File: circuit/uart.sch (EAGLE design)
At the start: 2 parts

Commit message: New circuit
Hopefully the final
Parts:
- added R3, R4: 1K, resistor:R-US_0204/5
- R1: value 4K7 -> 1K; device resistor:R-US_0204/7 -> resistor:R-US_0204/5
- R2: value 10K -> 1K; device resistor:R-US_0204/7 -> resistor:R-US_0204/5
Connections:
- removed net 0V: R1.1, R2.1
- new net GND: R2.1, R4.1
- new net N$2: R1.1, R2.2
- new net N$3: R3.2
- new net N$4: R3.1, R4.2
- net N$1: no longer R2.2
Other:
- note added: "AVR RX"
- note added: "AVR TX"
- note added: "RaspberryPi RX"
- note added: "RaspberryPi TX"
- note removed: "Metal contacts"
- note removed: "ONEWIRE_P"
- note removed: "onewire_pins[]"
- note removed: "station"
- note removed: "train"
- moved on the sheet: R1, R2
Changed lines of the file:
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@@
 </classes>
 <parts>
-<part name="R1" library="resistor" deviceset="R-US_" device="0204/7" value="4K7"/>
-<part name="R2" library="resistor" deviceset="R-US_" device="0204/7" value="10K"/>
-<part name="GND1" library="supply1" deviceset="0V" device=""/>
-<part name="GND2" library="supply1" deviceset="0V" device=""/>
+<part name="R1" library="resistor" deviceset="R-US_" device="0204/5" value="1K"/>
+<part name="R2" library="resistor" deviceset="R-US_" device="0204/5" value="1K"/>
+<part name="R3" library="resistor" deviceset="R-US_" device="0204/5" value="1K"/>
+<part name="R4" library="resistor" deviceset="R-US_" device="0204/5" value="1K"/>
+<part name="GND1" library="supply1" deviceset="GND" device=""/>
+<part name="GND2" library="supply1" deviceset="GND" device=""/>
 <part name="SUPPLY1" library="supply2" deviceset="V--&gt;" device=""/>
-<part name="SUPPLY2" library="supply2" deviceset="V&lt;--" device=""/>
+<part name="SUPPLY2" library="supply2" deviceset="V--&gt;" device=""/>
+<part name="SUPPLY3" library="supply2" deviceset="V&lt;--" device=""/>
+<part name="SUPPLY4" library="supply2" deviceset="V&lt;--" device=""/>
 </parts>
 <sheets>
 <sheet>
 <plain>
-<text x="33.02" y="68.58" size="1.778" layer="97">ONEWIRE_P</text>
-<text x="-30.48" y="68.58" size="1.778" layer="97">onewire_pins[]</text>
-<text x="0" y="66.04" size="1.778" layer="97">Metal contacts</text>
-<text x="-27.94" y="60.96" size="1.778" layer="97">station</text>
-<text x="38.1" y="60.96" size="1.778" layer="97">train</text>
+<text x="22.86" y="76.2" size="1.778" layer="97">AVR TX</text>
+<text x="22.86" y="33.02" size="1.778" layer="97">AVR RX</text>
+<text x="63.5" y="15.24" size="1.778" layer="97">RaspberryPi TX</text>
+<text x="60.96" y="58.42" size="1.778" layer="97">RaspberryPi RX</text>
 </plain>
 <instances>
-<instance part="R1" gate="G$1" x="-7.62" y="58.42" rot="R90"/>
-<instance part="R2" gate="G$1" x="22.86" y="58.42" rot="R90"/>
-<instance part="GND1" gate="1" x="-7.62" y="45.72"/>
-<instance part="GND2" gate="1" x="22.86" y="45.72"/>
-<instance part="SUPPLY1" gate="G$1" x="-30.48" y="66.04"/>
-<instance part="SUPPLY2" gate="G$1" x="48.26" y="66.04"/>
+<instance part="R1" gate="G$1" x="50.8" y="63.5" rot="R90"/>
+<instance part="R2" gate="G$1" x="50.8" y="48.26" rot="R90"/>
+<instance part="R3" gate="G$1" x="50.8" y="20.32" rot="R90"/>
+<instance part="R4" gate="G$1" x="50.8" y="5.08" rot="R90"/>
+<instance part="GND1" gate="1" x="50.8" y="35.56"/>
+<instance part="GND2" gate="1" x="50.8" y="-7.62"/>
+<instance part="SUPPLY1" gate="G$1" x="20.32" y="73.66"/>
+<instance part="SUPPLY2" gate="G$1" x="20.32" y="30.48"/>
+<instance part="SUPPLY3" gate="G$1" x="78.74" y="12.7"/>
+<instance part="SUPPLY4" gate="G$1" x="76.2" y="55.88"/>
 </instances>
 <busses>
@@
 <net name="N$1" class="0">
 <segment>
-<wire x1="-15.24" y1="66.04" x2="-7.62" y2="66.04" width="0.1524" layer="91"/>
 <pinref part="R1" gate="G$1" pin="2"/>
-<wire x1="33.02" y1="66.04" x2="22.86" y2="66.04" width="0.1524" layer="91"/>
-<wire x1="22.86" y1="66.04" x2="-7.62" y2="66.04" width="0.1524" layer="91"/>
-<wire x1="-7.62" y1="66.04" x2="-7.62" y2="63.5" width="0.1524" layer="91"/>
-<pinref part="R2" gate="G$1" pin="2"/>
-<wire x1="22.86" y1="66.04" x2="22.86" y2="63.5" width="0.1524" layer="91"/>
-<junction x="22.86" y="66.04"/>
-<junction x="-7.62" y="66.04"/>
+<wire x1="35.56" y1="73.66" x2="50.8" y2="73.66" width="0.1524" layer="91"/>
+<wire x1="50.8" y1="73.66" x2="50.8" y2="68.58" width="0.1524" layer="91"/>
 </segment>
 </net>
-<net name="0V" class="0">
+<net name="N$2" class="0">
 <segment>
 <pinref part="R1" gate="G$1" pin="1"/>
-<pinref part="GND1" gate="1" pin="0V"/>
-<wire x1="-7.62" y1="53.34" x2="-7.62" y2="48.26" width="0.1524" layer="91"/>
+<pinref part="R2" gate="G$1" pin="2"/>
+<wire x1="50.8" y1="58.42" x2="50.8" y2="55.88" width="0.1524" layer="91"/>
+<wire x1="50.8" y1="55.88" x2="50.8" y2="53.34" width="0.1524" layer="91"/>
+<wire x1="60.96" y1="55.88" x2="50.8" y2="55.88" width="0.1524" layer="91"/>
+<junction x="50.8" y="55.88"/>
+</segment>
+</net>
+<net name="GND" class="0">
+<segment>
+<pinref part="R2" gate="G$1" pin="1"/>
+<pinref part="GND1" gate="1" pin="GND"/>
+<wire x1="50.8" y1="43.18" x2="50.8" y2="38.1" width="0.1524" layer="91"/>
 </segment>
 <segment>
-<pinref part="R2" gate="G$1" pin="1"/>
-<pinref part="GND2" gate="1" pin="0V"/>
-<wire x1="22.86" y1="53.34" x2="22.86" y2="48.26" width="0.1524" layer="91"/>
+<pinref part="R4" gate="G$1" pin="1"/>
+<pinref part="GND2" gate="1" pin="GND"/>
+<wire x1="50.8" y1="0" x2="50.8" y2="-5.08" width="0.1524" layer="91"/>
 </segment>
 </net>
+<net name="N$3" class="0">
+<segment>
+<pinref part="R3" gate="G$1" pin="2"/>
+<wire x1="50.8" y1="25.4" x2="50.8" y2="30.48" width="0.1524" layer="91"/>
+<wire x1="50.8" y1="30.48" x2="35.56" y2="30.48" width="0.1524" layer="91"/>
+</segment>
+</net>
+<net name="N$4" class="0">
+<segment>
+<pinref part="R3" gate="G$1" pin="1"/>
+<pinref part="R4" gate="G$1" pin="2"/>
+<wire x1="50.8" y1="15.24" x2="50.8" y2="12.7" width="0.1524" layer="91"/>
+<wire x1="50.8" y1="12.7" x2="50.8" y2="10.16" width="0.1524" layer="91"/>
+<wire x1="63.5" y1="12.7" x2="50.8" y2="12.7" width="0.1524" layer="91"/>
+<junction x="50.8" y="12.7"/>
+</segment>
+</net>

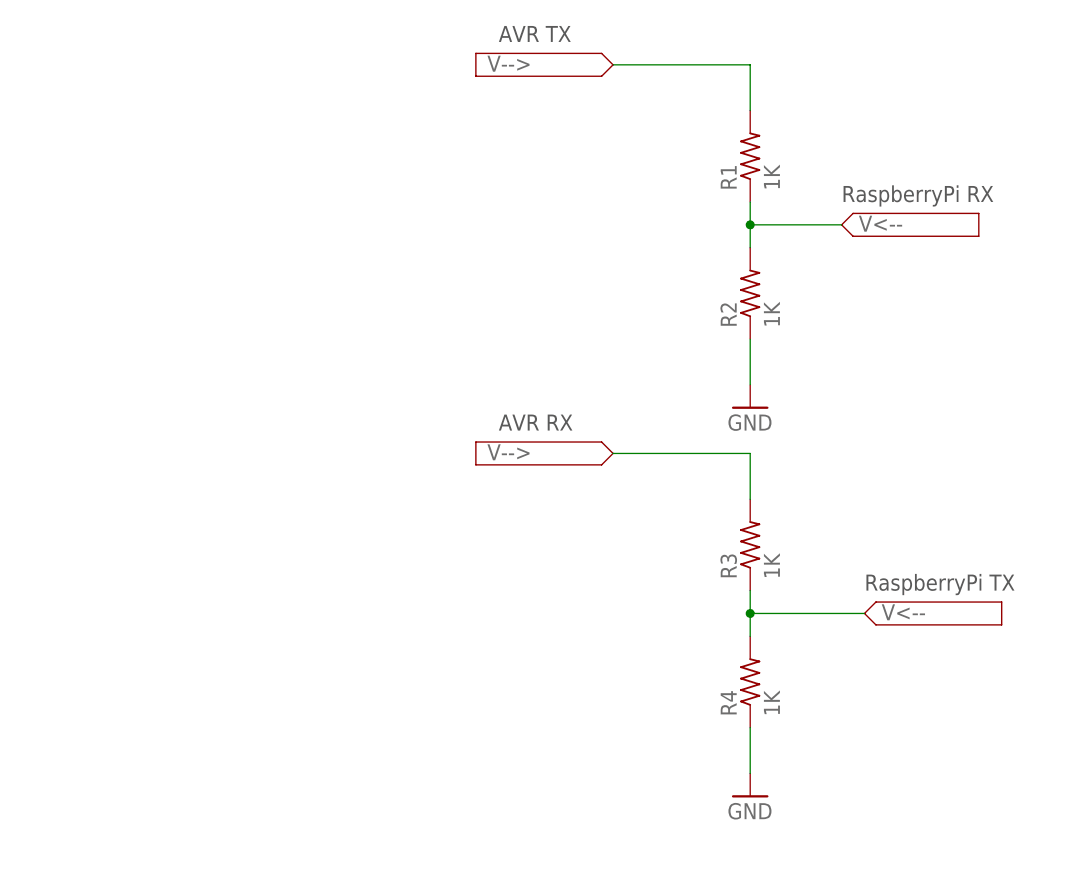
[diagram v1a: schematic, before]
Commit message: New UART circuit
Using CD4050 IC
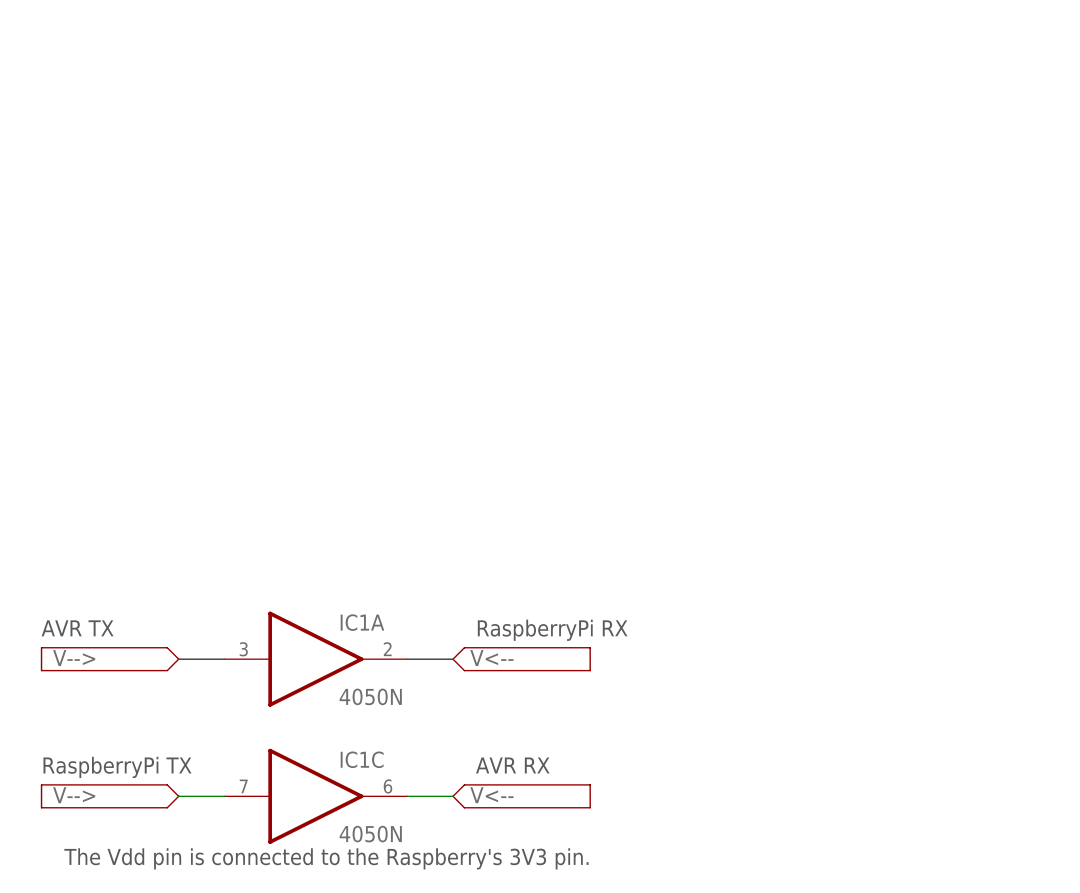
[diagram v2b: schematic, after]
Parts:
- removed R1, R2, R3, R4: 1K, resistor:R-US_0204/5
- added IC1: 4050N, 40xx:4050N
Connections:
- removed net GND: R2.1, R4.1
- net N$1: now also IC1A.I; no longer R1.2
- net N$2: now also IC1C.I; no longer R1.1, R2.2
- net N$3: now also IC1A.O; no longer R3.2
- net N$4: now also IC1C.O; no longer R3.1, R4.2
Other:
- note added: "The Vdd pin is connected to the Raspberry's 3V3 pin."
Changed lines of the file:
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@@
 <setting verticaltext="up"/>
 </settings>
-<grid distance="0.1" unitdist="inch" unit="inch" style="lines" multiple="1" display="no" altdistance="0.01" altunitdist="inch" altunit="inch"/>
+<grid distance="0.1" unitdist="inch" unit="inch" style="lines" multiple="1" display="yes" altdistance="0.01" altunitdist="inch" altunit="inch"/>
 <layers>
 <layer number="1" name="Top" color="4" fill="1" visible="no" active="no"/>
@@
 </classes>
 <parts>
-<part name="R1" library="resistor" deviceset="R-US_" device="0204/5" value="1K"/>
-<part name="R2" library="resistor" deviceset="R-US_" device="0204/5" value="1K"/>
-<part name="R3" library="resistor" deviceset="R-US_" device="0204/5" value="1K"/>
-<part name="R4" library="resistor" deviceset="R-US_" device="0204/5" value="1K"/>
-<part name="GND1" library="supply1" deviceset="GND" device=""/>
-<part name="GND2" library="supply1" deviceset="GND" device=""/>
 <part name="SUPPLY1" library="supply2" deviceset="V--&gt;" device=""/>
 <part name="SUPPLY2" library="supply2" deviceset="V--&gt;" device=""/>
 <part name="SUPPLY3" library="supply2" deviceset="V&lt;--" device=""/>
 <part name="SUPPLY4" library="supply2" deviceset="V&lt;--" device=""/>
+<part name="IC1" library="40xx" deviceset="4050" device="N"/>
 </parts>
 <sheets>
 <sheet>
 <plain>
-<text x="22.86" y="76.2" size="1.778" layer="97">AVR TX</text>
-<text x="22.86" y="33.02" size="1.778" layer="97">AVR RX</text>
-<text x="63.5" y="15.24" size="1.778" layer="97">RaspberryPi TX</text>
-<text x="60.96" y="58.42" size="1.778" layer="97">RaspberryPi RX</text>
+<text x="-27.94" y="10.16" size="1.778" layer="97">AVR TX</text>
+<text x="20.32" y="-5.08" size="1.778" layer="97">AVR RX</text>
+<text x="-27.94" y="-5.08" size="1.778" layer="97">RaspberryPi TX</text>
+<text x="20.32" y="10.16" size="1.778" layer="97">RaspberryPi RX</text>
+<text x="-25.4" y="-15.24" size="1.778" layer="97">The Vdd pin is connected to the Raspberry's 3V3 pin.</text>
 </plain>
 <instances>
-<instance part="R1" gate="G$1" x="50.8" y="63.5" rot="R90"/>
-<instance part="R2" gate="G$1" x="50.8" y="48.26" rot="R90"/>
-<instance part="R3" gate="G$1" x="50.8" y="20.32" rot="R90"/>
-<instance part="R4" gate="G$1" x="50.8" y="5.08" rot="R90"/>
-<instance part="GND1" gate="1" x="50.8" y="35.56"/>
-<instance part="GND2" gate="1" x="50.8" y="-7.62"/>
-<instance part="SUPPLY1" gate="G$1" x="20.32" y="73.66"/>
-<instance part="SUPPLY2" gate="G$1" x="20.32" y="30.48"/>
-<instance part="SUPPLY3" gate="G$1" x="78.74" y="12.7"/>
-<instance part="SUPPLY4" gate="G$1" x="76.2" y="55.88"/>
+<instance part="SUPPLY1" gate="G$1" x="-27.94" y="7.62"/>
+<instance part="SUPPLY2" gate="G$1" x="-27.94" y="-7.62"/>
+<instance part="SUPPLY3" gate="G$1" x="33.02" y="-7.62"/>
+<instance part="SUPPLY4" gate="G$1" x="33.02" y="7.62"/>
+<instance part="IC1" gate="A" x="2.54" y="7.62"/>
+<instance part="IC1" gate="C" x="2.54" y="-7.62"/>
 </instances>
 <busses>
@@
 <net name="N$1" class="0">
 <segment>
-<pinref part="R1" gate="G$1" pin="2"/>
-<wire x1="35.56" y1="73.66" x2="50.8" y2="73.66" width="0.1524" layer="91"/>
-<wire x1="50.8" y1="73.66" x2="50.8" y2="68.58" width="0.1524" layer="91"/>
+<pinref part="IC1" gate="A" pin="I"/>
+<wire x1="-12.7" y1="7.62" x2="-7.62" y2="7.62" width="0.1524" layer="91"/>
 </segment>
 </net>
 <net name="N$2" class="0">
 <segment>
-<pinref part="R1" gate="G$1" pin="1"/>
-<pinref part="R2" gate="G$1" pin="2"/>
-<wire x1="50.8" y1="58.42" x2="50.8" y2="55.88" width="0.1524" layer="91"/>
-<wire x1="50.8" y1="55.88" x2="50.8" y2="53.34" width="0.1524" layer="91"/>
-<wire x1="60.96" y1="55.88" x2="50.8" y2="55.88" width="0.1524" layer="91"/>
-<junction x="50.8" y="55.88"/>
-</segment>
-</net>
-<net name="GND" class="0">
-<segment>
-<pinref part="R2" gate="G$1" pin="1"/>
-<pinref part="GND1" gate="1" pin="GND"/>
-<wire x1="50.8" y1="43.18" x2="50.8" y2="38.1" width="0.1524" layer="91"/>
-</segment>
-<segment>
-<pinref part="R4" gate="G$1" pin="1"/>
-<pinref part="GND2" gate="1" pin="GND"/>
-<wire x1="50.8" y1="0" x2="50.8" y2="-5.08" width="0.1524" layer="91"/>
+<pinref part="IC1" gate="C" pin="I"/>
+<wire x1="-12.7" y1="-7.62" x2="-7.62" y2="-7.62" width="0.1524" layer="91"/>
 </segment>
 </net>
 <net name="N$3" class="0">
 <segment>
-<pinref part="R3" gate="G$1" pin="2"/>
-<wire x1="50.8" y1="25.4" x2="50.8" y2="30.48" width="0.1524" layer="91"/>
-<wire x1="50.8" y1="30.48" x2="35.56" y2="30.48" width="0.1524" layer="91"/>
+<pinref part="IC1" gate="A" pin="O"/>
+<wire x1="12.7" y1="7.62" x2="17.78" y2="7.62" width="0.1524" layer="91"/>
 </segment>
 </net>
 <net name="N$4" class="0">
 <segment>
-<pinref part="R3" gate="G$1" pin="1"/>
-<pinref part="R4" gate="G$1" pin="2"/>
-<wire x1="50.8" y1="15.24" x2="50.8" y2="12.7" width="0.1524" layer="91"/>
-<wire x1="50.8" y1="12.7" x2="50.8" y2="10.16" width="0.1524" layer="91"/>
-<wire x1="63.5" y1="12.7" x2="50.8" y2="12.7" width="0.1524" layer="91"/>
-<junction x="50.8" y="12.7"/>
+<pinref part="IC1" gate="C" pin="O"/>
+<wire x1="12.7" y1="-7.62" x2="17.78" y2="-7.62" width="0.1524" layer="91"/>
 </segment>
 </net>
